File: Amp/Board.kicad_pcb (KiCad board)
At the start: 2 copper layers, 22 parts, among them J1 *SDNL/5V, J10 OUTR_1, J12 12V in, J2 IN_1, J3 OUTL_1, J6 THERM, J8 Gain_Conn, U1 SSM3302ACPZ-R7

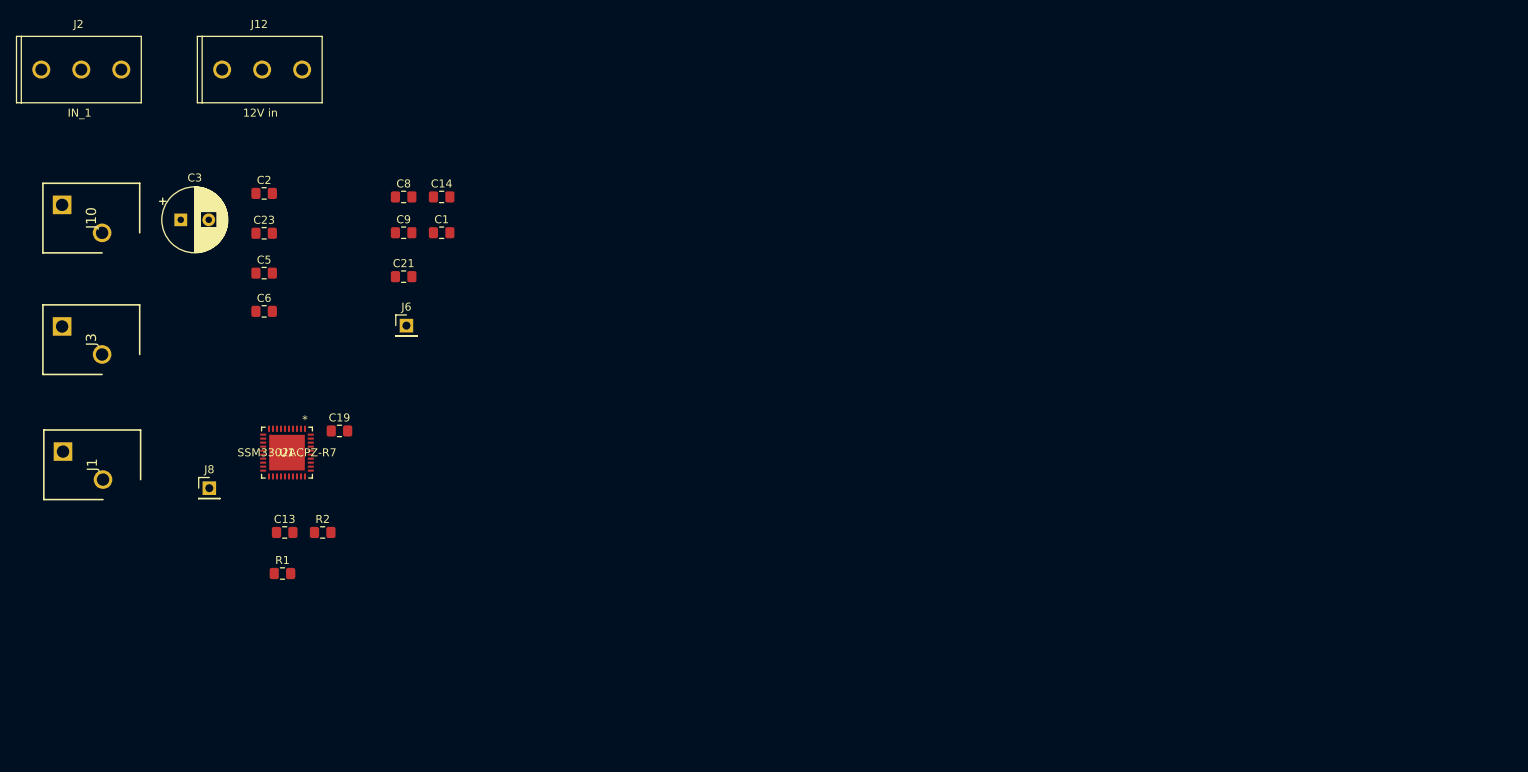
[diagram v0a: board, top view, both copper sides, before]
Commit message: finished DSP and AMP
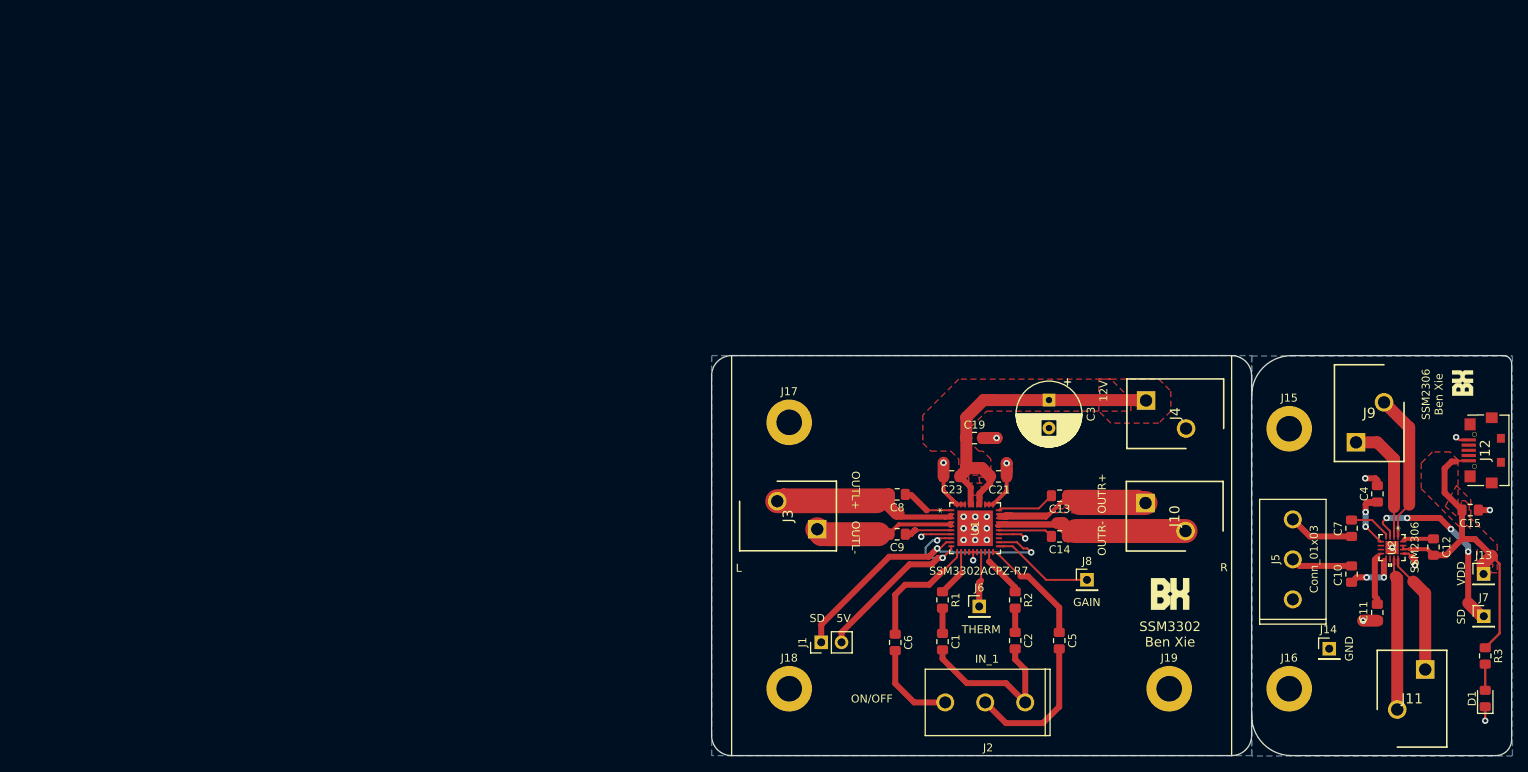
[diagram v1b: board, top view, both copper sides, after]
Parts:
- added C10: 22nF, Capacitor_SMD:C_0805_2012Metric_Pad1.15x1.40mm_HandSolder, F.Cu at (175.3, 85.7)
- added C11: 22nF, Capacitor_SMD:C_0805_2012Metric_Pad1.15x1.40mm_HandSolder, F.Cu at (178.5, 90.5)
- added C12: .1uF, Capacitor_SMD:C_0805_2012Metric_Pad1.15x1.40mm_HandSolder, F.Cu at (185.5, 82.3)
- added C15: 10uF, Capacitor_SMD:C_0805_2012Metric_Pad1.15x1.40mm_HandSolder, F.Cu at (190.1, 77.7)
- added C4: 22nF, Capacitor_SMD:C_0805_2012Metric_Pad1.15x1.40mm_HandSolder, F.Cu at (178.5, 75.6)
- added C7: 22nF, Capacitor_SMD:C_0805_2012Metric_Pad1.15x1.40mm_HandSolder, F.Cu at (175.3, 79.9)
- added D1: LED, LED_SMD:LED_0805_2012Metric_Pad1.15x1.40mm_HandSolder, F.Cu at (192.0, 101.2)
- added G***: LOGO, logo:logo_5mm, F.Cu at (189.2, 61.8)
- added G***: LOGO, logo:logo_7_5mm, F.Cu at (152.6, 88.2)
- added J11: Conn_01x02_Female, WJ250A-3.50-2P:WJ250A3502P, F.Cu at (184.5, 97.6)
- added J13: Conn_01x01_Female, Connector_PinHeader_2.54mm:PinHeader_1x01_P2.54mm_Vertical, F.Cu at (191.8, 85.7)
- added J14: Conn_01x01_Female, Connector_PinHeader_2.54mm:PinHeader_1x01_P2.54mm_Vertical, F.Cu at (172.5, 95.0)
- added J15: Conn_01x01_Female, MountingHole:MountingHole_3.2mm_M3_ISO7380_Pad, F.Cu at (167.5, 67.5)
- added J16: Conn_01x01_Female, MountingHole:MountingHole_3.2mm_M3_ISO7380_Pad, F.Cu at (167.5, 100.0)
- added J17: Conn_01x01_Female, MountingHole:MountingHole_3.2mm_M3_ISO7380_Pad, F.Cu at (105.0, 66.7)
- added J18: Conn_01x01_Female, MountingHole:MountingHole_3.2mm_M3_ISO7380_Pad, F.Cu at (105.0, 100.0)
- added J19: Conn_01x01_Female, MountingHole:MountingHole_3.2mm_M3_ISO7380_Pad, F.Cu at (152.5, 100.0)
- added J4: 12V, WJ250A-3.50-2P:WJ250A3502P, F.Cu at (149.6, 64.0)
- added J5: Conn_01x03, 691213710003:691213710003, F.Cu at (167.9, 83.8)
- added J7: SD, Connector_PinHeader_2.54mm:PinHeader_1x01_P2.54mm_Vertical, F.Cu at (191.8, 90.9)
- added J9: Conn_01x02_Female, WJ250A-3.50-2P:WJ250A3502P, F.Cu at (175.8, 69.2)
- added R3: 100R, Resistor_SMD:R_0805_2012Metric_Pad1.15x1.40mm_HandSolder, F.Cu at (192.0, 95.9)
- added U2: SSM2306, SSM2306:SSM2306CPZ-REEL7, F.Cu at (180.3, 82.4)
- J1: value *SDNL/5V -> *SD/5V; footprint WJ250A-3.50-2P:WJ250A3502P -> Connector_PinHeader_2.54mm:PinHeader_1x02_P2.54mm_Vertical
- J12: value 12V in -> USB_B_Micro; footprint 691213710003:691213710003 -> MicroUSB:C77238
- moved J12 160.1 mm to (192.0, 70.2), turned to 90 degrees
- moved J10 140.5 mm to (149.5, 76.8)
- moved J2 137.9 mm to (129.5, 101.7), turned to 180 degrees
- moved C3 110.8 mm to (137.5, 63.9), turned to 270 degrees
- moved J8 110.3 mm to (142.2, 86.4)
- moved C5 109.5 mm to (138.8, 94.0), turned to 270 degrees
- moved C2 109.3 mm to (133.2, 94.0), turned to 270 degrees
- moved J3 97.7 mm to (108.5, 80.1), turned to 270 degrees
- moved J1 97.7 mm to (109.0, 94.2)
- moved C13 97.0 mm to (138.8, 75.9), turned to 180 degrees
- moved C23 91.2 mm to (125.3, 73.5), turned to 180 degrees
- moved C6 89.1 mm to (118.2, 94.2), turned to 270 degrees
- moved C14 88.1 mm to (138.8, 81.0), turned to 180 degrees
- moved R2 87.0 mm to (133.2, 88.9), turned to 270 degrees
- moved U1 86.5 mm to (128.2, 79.9), turned to 90 degrees
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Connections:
- J12 pad 1: +12V -> VDD
- J12 pad 2: GND -> Net-(J12-Pad2)
- J12 pad 3: GND -> Net-(J12-Pad3)
- U1 pad 22: /AMP_PWR -> Net-(J1-Pad1)
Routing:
- net Net-(C14-Pad1): track 0.00 -> 50.7 mm
- net GND: track 0.00 -> 46.6 mm, vias 0 -> 15
- net Net-(C8-Pad2): track 0.00 -> 43.6 mm
- net +12V: track 0.00 -> 42.8 mm
- net VDD: track 0.00 -> 42.0 mm
- net Net-(J1-Pad1): track 0.00 -> 39.2 mm, vias 0 -> 2
- net Net-(C13-Pad1): track 0.00 -> 38.2 mm
- net Net-(J1-Pad2): track 0.00 -> 26.7 mm, vias 0 -> 2
- net Net-(C9-Pad2): track 0.00 -> 25.3 mm
- net Net-(J7-Pad1): track 0.00 -> 24.9 mm, vias 0 -> 4
- net Net-(J11-Pad2): track 0.00 -> 19.0 mm
- net Net-(J9-Pad2): track 0.00 -> 18.6 mm
- net Net-(C5-Pad2): track 0.00 -> 18.4 mm
- net GNDREF: track 0.00 -> 16.1 mm, vias 0 -> 7
- net Net-(C6-Pad1): track 0.00 -> 15.5 mm
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- added copper zone on F.Cu, net +12V
- added copper zone on B.Cu, net GND
- added copper zone on B.Cu, net GNDREF
- added copper zone on F.Cu, net Net-(C13-Pad1)
- added copper zone on F.Cu, net VDD
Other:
- board outline added: 100 x 50 mm
- net class Default: clearance 0.2 -> 0.1
- rule trace_clearance: 0.2 -> 0.1
- board text added: "12V"
- board text added: "50 x 32.6 mm 32.5 mm 01/20"
- board text added: "5V"
- board text added: "68 x 50 mm 50 x 33.3 mm 01/20"
- board text added: "GAIN"
- board text added: "GND"
- board text added: "L"
- board text added: "ON/OFF"
- board text added: "OUTL+"
- board text added: "OUTL-"
- board text added: "OUTR+"
- board text added: "OUTR-"
- board text added: "R"
- board text added: "SD"
- board text added: "SSM2306 Ben Xie"
- board text added: "SSM3302 Ben Xie"
- board text added: "THERM"
- board text added: "VDD"
